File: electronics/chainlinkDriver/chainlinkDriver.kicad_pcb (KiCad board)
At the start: 2 copper layers, 198.1 x 30.5 mm, 66 parts, among them J10 Sensor, J11 Sensor, J12 Motor, J13 Motor, J14 Sensor, J15 Sensor, J16 Power, J17 Power, J18 Power, J19 IDC, J20 IDC, J3 Motor, J5 Motor, J6 Motor, J7 Motor, J8 Sensor, J9 Sensor, U1 74HC595, U10 TPL7407L, U2 TPL7407L, U3 74HC125, U4 74HC165, U5 74HC595, U6 TPL7407L, U7 74HC595, U8 TPL7407L, U9 74HC595

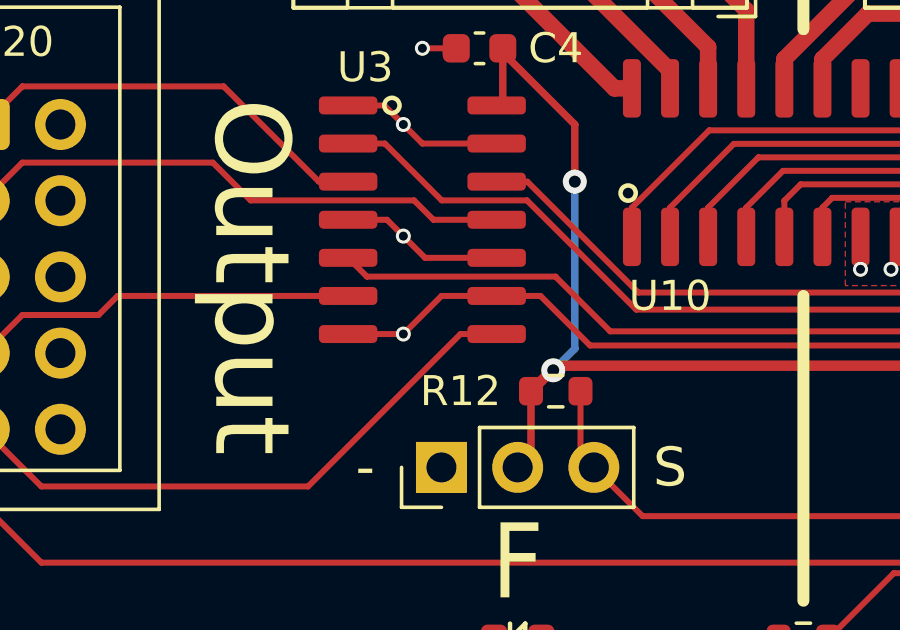
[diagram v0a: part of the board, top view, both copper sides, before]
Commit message: More tweaks to Chainlink Driver, update Chainlink Buddy
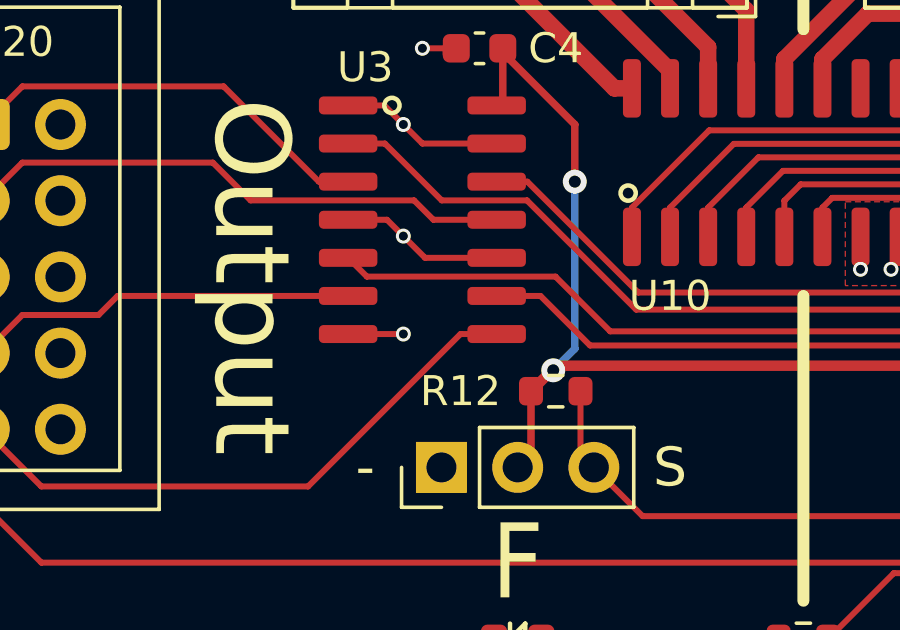
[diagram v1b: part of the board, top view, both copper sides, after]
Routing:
- net GND: track 76.1 -> 72.5 mm
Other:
- board text added: "For compatibility with older Chainlink PCBs, use 2x4 IDC connector in highlighted location."
- board text added: "v1.5"
- board text removed: "v1.2"

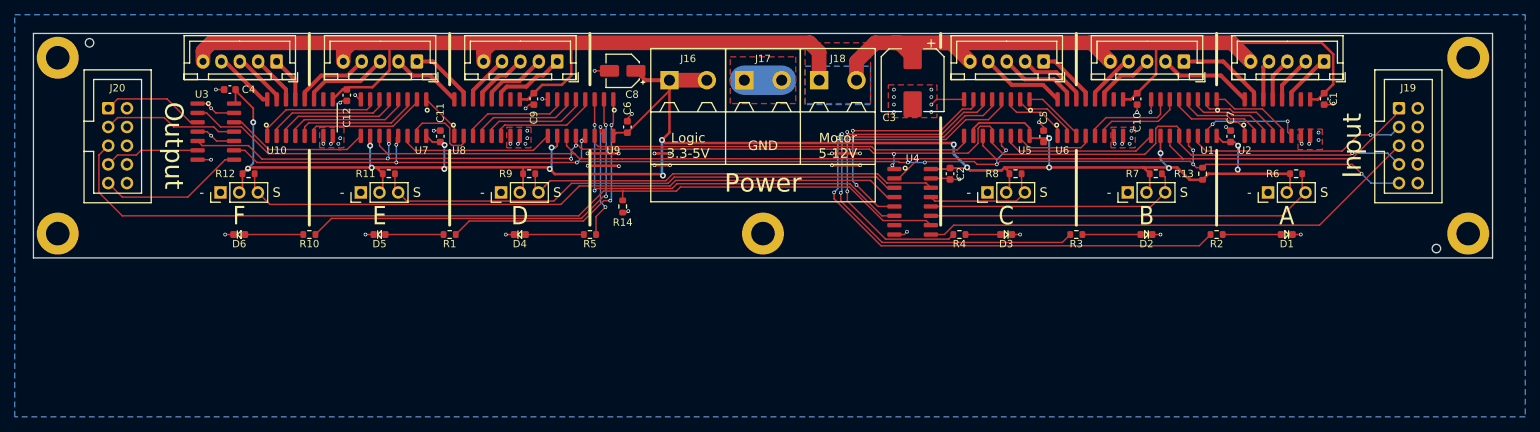
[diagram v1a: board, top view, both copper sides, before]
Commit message: Started shifting connectors outward, locking header pin footprint
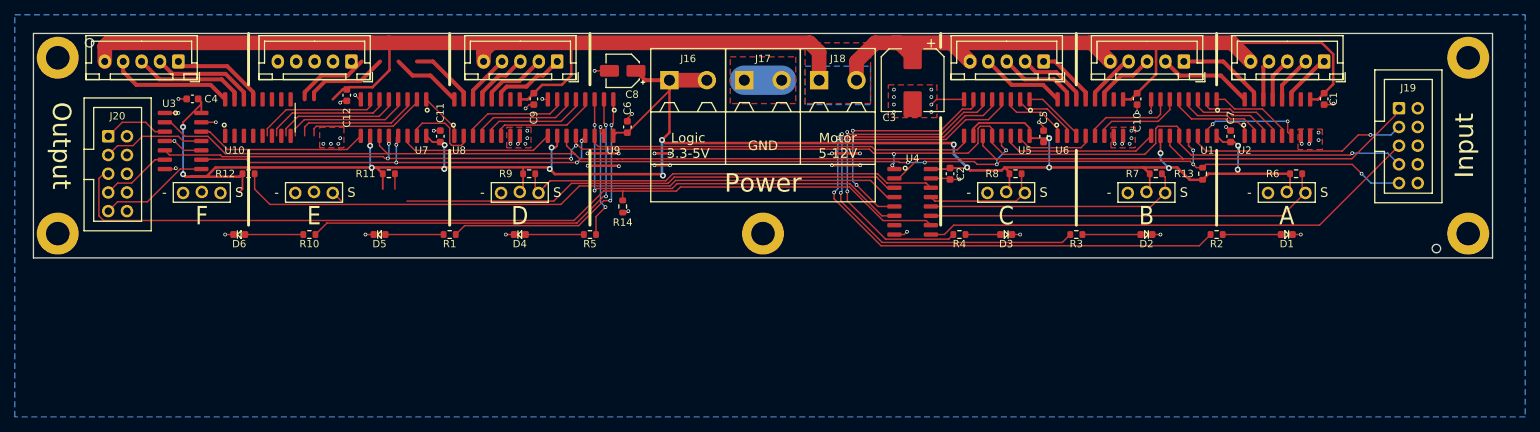
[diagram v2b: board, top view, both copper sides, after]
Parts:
- J10, J11, J14, J15, J8, J9: footprint Connector_PinHeader_2.54mm:PinHeader_1x03_P2.54mm_Vertical -> ModifiedSymbols:PinHeader_1x03_P2.54mm_Vertical_Locking
- moved J13 13.3 mm to (45.1, 29.2)
- moved J12 8.89 mm to (68.6, 29.2)
- moved J14 8.89 mm to (61.0, 47.0)
- moved U10 5.71 mm to (55.9, 36.8)
- moved C4 5.24 mm to (47.0, 34.3)
- moved J15 5.08 mm to (45.7, 47.0)
- moved U3 4.62 mm to (45.7, 40.0)
- moved J20 3.81 mm to (35.6, 39.4)
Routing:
- net +3V3: track 268.2 -> 282.3 mm
- net +12V: track 226.3 -> 237.0 mm
- net /OUT_F_PHASE_D: track 8.36 -> 16.8 mm
- net /OUT_F_PHASE_C: track 7.48 -> 15.3 mm
- net /OUT_F_PHASE_B: track 6.71 -> 14.1 mm
- net /OUT_F_PHASE_A: track 6.20 -> 12.9 mm
- net /CLOCK_OUT: track 14.0 -> 9.00 mm
- net /nOE_OUT: track 20.0 -> 15.0 mm
- net /MOTOR_OUT: track 18.4 -> 14.0 mm
- net /nOE_IN: track 177.2 -> 181.5 mm
- net /MOTOR_OUT_PRE_BUFFER: track 19.9 -> 23.8 mm
- net /CLOCK_IN: track 189.0 -> 192.9 mm
- net /LATCH_IN: track 185.9 -> 189.7 mm
- net /LATCH_OUT: track 12.9 -> 9.53 mm
- net GND: track 72.5 -> 70.5 mm, vias 63 -> 64
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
